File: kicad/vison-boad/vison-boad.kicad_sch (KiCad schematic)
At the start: 29 parts, among them J1 USB_C_Receptacle_USB2.0, J2 Wio Terminal, J3 UART, J4 pin_test, J5 NEO PIXEL, J6 to main, J7 I2C_0, SW1 BOOTSET, SW2 RESET, SW3 M1n_RST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

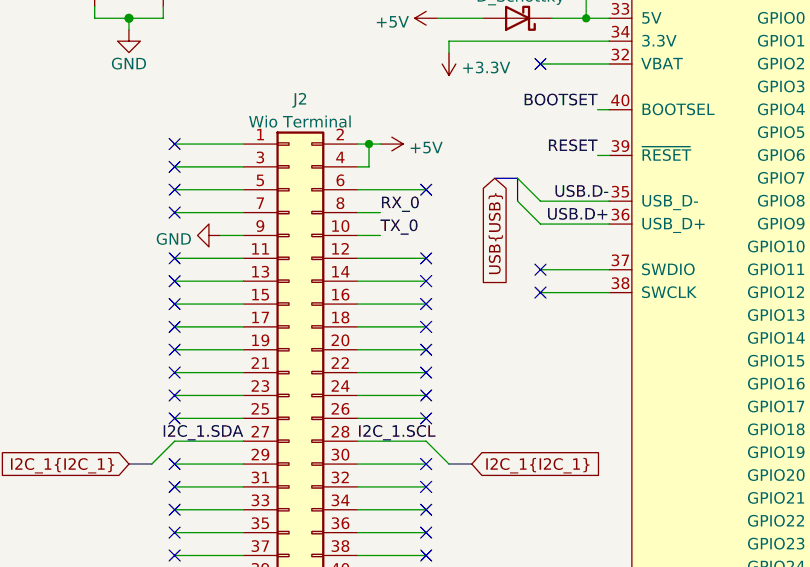
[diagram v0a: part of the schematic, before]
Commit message: Add GND to Wio pin14
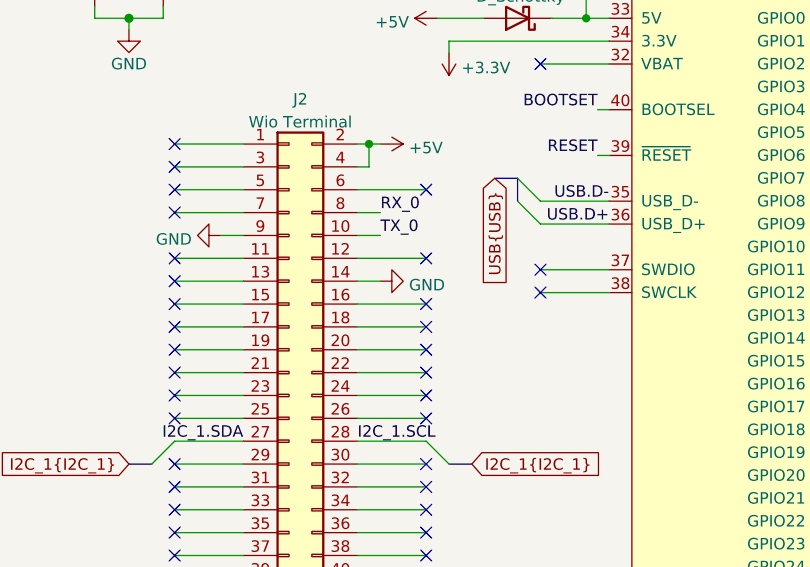
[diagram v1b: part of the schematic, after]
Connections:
- net GND: now also J2.14 (Pin_14)
- no-connect marks 234 -> 233
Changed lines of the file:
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@@
   (no_connect (at 181.61 100.33))
   (no_connect (at 33.02 86.36))
-  (no_connect (at 60.96 93.98))
   (no_connect (at 33.02 96.52))
   (no_connect (at 181.61 120.65))
@@
     (stroke (width 0) (type solid) (color 0 0 0 0))
   )
-  (wire (pts (xy 53.34 93.98) (xy 60.96 93.98))
+  (wire (pts (xy 53.34 93.98) (xy 55.88 93.98))
     (stroke (width 0) (type default) (color 0 0 0 0))
   )
@@
     (pin "1")
   )
+  (symbol (lib_id "power:GND") (at 55.88 93.98 90) (unit 1)
+    (in_bom yes) (on_board yes) (fields_autoplaced)
+    (property "Reference" "#PWR?" (id 0) (at 62.23 93.98 0)
+      (effects (font (size 1.27 1.27)) hide)
+    )
+    (property "Value" "GND" (id 1) (at 59.055 94.4138 90)
+      (effects (font (size 1.27 1.27)) (justify right))
+    )
+    (property "Footprint" "" (id 2) (at 55.88 93.98 0)
+      (effects (font (size 1.27 1.27)) hide)
+    )
+    (property "Datasheet" "" (id 3) (at 55.88 93.98 0)
+      (effects (font (size 1.27 1.27)) hide)
+    )
+    (pin "1")
+  )
   (symbol (lib_id "power:+3.3V") (at 82.55 179.07 0) (unit 1)
     (in_bom yes) (on_board yes) (fields_autoplaced)
@@
       (reference "#PWR0101") (unit 1) (value "+3.3V") (footprint "")
     )
+    (path "/143cc9c2-ef1a-4bb5-b72d-2764ac3b48c3"
+      (reference "#PWR?") (unit 1) (value "GND") (footprint "")
+    )
     (path "/31be8863-1987-4197-85f1-2ca80d5b7afb"
